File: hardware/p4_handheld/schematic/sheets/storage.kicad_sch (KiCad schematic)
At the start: 0 parts

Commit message: hw(p4_handheld): audio, storage, debug sheets
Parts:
- added J4: microSD-pushpush, TF-015, symbol PSP4H:Block2
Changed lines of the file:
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@@
     (comment 2 "Same-net labels connect; globals cross sheets")
   )
+  (symbol (lib_id "PSP4H:Block2") (at 35 35 0) (unit 1)
+    (exclude_from_sim no) (in_bom yes) (on_board yes) (dnp no) (fields_autoplaced)
+    (property "Reference" "J4" (at 35 29 0)
+      (effects (font (size 1.27 1.27))))
+    (property "Value" "microSD-pushpush" (at 35 41 0)
+      (effects (font (size 1.27 1.27))))
+    (property "Footprint" "TF-015" (at 35 35 0)
+      (effects (font (size 1.27 1.27)) hide))
+    (property "Datasheet" "~" (at 35 35 0)
+      (effects (font (size 1.27 1.27)) hide))
+    (property "Gate" "GATE-MICROSD-FOOTPRINT" (at 35 35 0)
+      (effects (font (size 1.27 1.27)) hide))
+    (property "LCSC" "C113206" (at 35 35 0)
+      (effects (font (size 1.27 1.27)) hide))
+    (property "MPN" "TF-015" (at 35 35 0)
+      (effects (font (size 1.27 1.27)) hide))
+    (instances (project "card" (path "/p4_handheld/sheets/storage" (reference "J4") (unit 1))))
+  )
+  (label "+3V3" (at 53 40 0) (fields_autoplaced)
+    (effects (font (size 1.27 1.27)) (justify left)))
+  (label "GND" (at 53 40 0) (fields_autoplaced)
+    (effects (font (size 1.27 1.27)) (justify left)))
+  (label "SD_D0" (at 53 30 0) (fields_autoplaced)
+    (effects (font (size 1.27 1.27)) (justify left)))
+  (label "SD_D1" (at 53 30 0) (fields_autoplaced)
+    (effects (font (size 1.27 1.27)) (justify left)))
+  (label "SD_D2" (at 53 30 0) (fields_autoplaced)
+    (effects (font (size 1.27 1.27)) (justify left)))
+  (label "SD_D3" (at 53 30 0) (fields_autoplaced)
+    (effects (font (size 1.27 1.27)) (justify left)))
+  (label "SD_CLK" (at 53 30 0) (fields_autoplaced)
+    (effects (font (size 1.27 1.27)) (justify left)))
+  (label "SD_CMD" (at 53 30 0) (fields_autoplaced)
+    (effects (font (size 1.27 1.27)) (justify left)))
+  (global_label "+3V3" (shape input) (at 280 20 0) (fields_autoplaced)
+    (effects (font (size 1.27 1.27)) (justify left))
+    (property "Intersheetrefs" "${INTERSHEET_REFS}" (at 280 20 0)
+      (effects (font (size 1.27 1.27)) hide))
+  )
+  (global_label "GND" (shape input) (at 280 26 0) (fields_autoplaced)
+    (effects (font (size 1.27 1.27)) (justify left))
+    (property "Intersheetrefs" "${INTERSHEET_REFS}" (at 280 26 0)
+      (effects (font (size 1.27 1.27)) hide))
+  )
+  (global_label "SD_D0" (shape input) (at 280 32 0) (fields_autoplaced)
+    (effects (font (size 1.27 1.27)) (justify left))
+    (property "Intersheetrefs" "${INTERSHEET_REFS}" (at 280 32 0)
+      (effects (font (size 1.27 1.27)) hide))
+  )
+  (global_label "SD_D1" (shape input) (at 280 38 0) (fields_autoplaced)
+    (effects (font (size 1.27 1.27)) (justify left))
+    (property "Intersheetrefs" "${INTERSHEET_REFS}" (at 280 38 0)
+      (effects (font (size 1.27 1.27)) hide))
+  )
+  (global_label "SD_D2" (shape input) (at 280 44 0) (fields_autoplaced)
+    (effects (font (size 1.27 1.27)) (justify left))
+    (property "Intersheetrefs" "${INTERSHEET_REFS}" (at 280 44 0)
+      (effects (font (size 1.27 1.27)) hide))
+  )
+  (global_label "SD_D3" (shape input) (at 280 50 0) (fields_autoplaced)
+    (effects (font (size 1.27 1.27)) (justify left))
+    (property "Intersheetrefs" "${INTERSHEET_REFS}" (at 280 50 0)
+      (effects (font (size 1.27 1.27)) hide))
+  )
+  (global_label "SD_CLK" (shape input) (at 280 56 0) (fields_autoplaced)
+    (effects (font (size 1.27 1.27)) (justify left))
+    (property "Intersheetrefs" "${INTERSHEET_REFS}" (at 280 56 0)
+      (effects (font (size 1.27 1.27)) hide))
+  )
+  (global_label "SD_CMD" (shape input) (at 280 62 0) (fields_autoplaced)
+    (effects (font (size 1.27 1.27)) (justify left))
+    (property "Intersheetrefs" "${INTERSHEET_REFS}" (at 280 62 0)
+      (effects (font (size 1.27 1.27)) hide))
+  )
 )

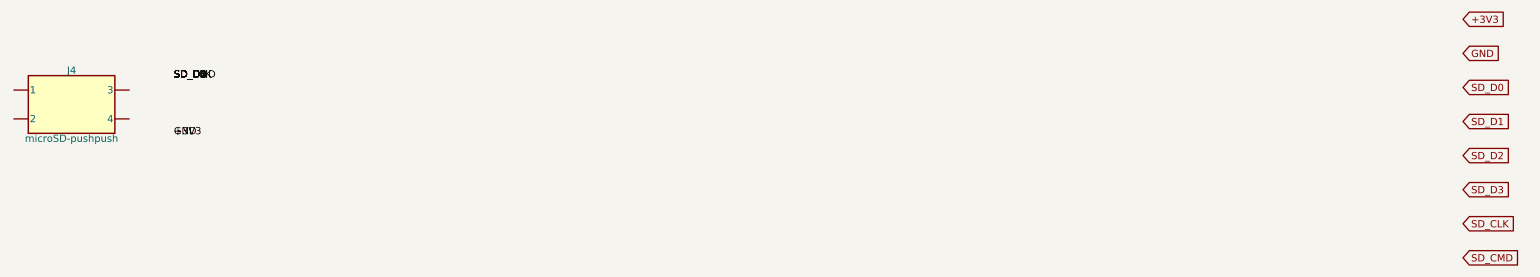
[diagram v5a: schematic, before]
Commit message: hw(p4_handheld): ERC-clean schematic engine (real pins, on-endpoint labels, project symbol lib)
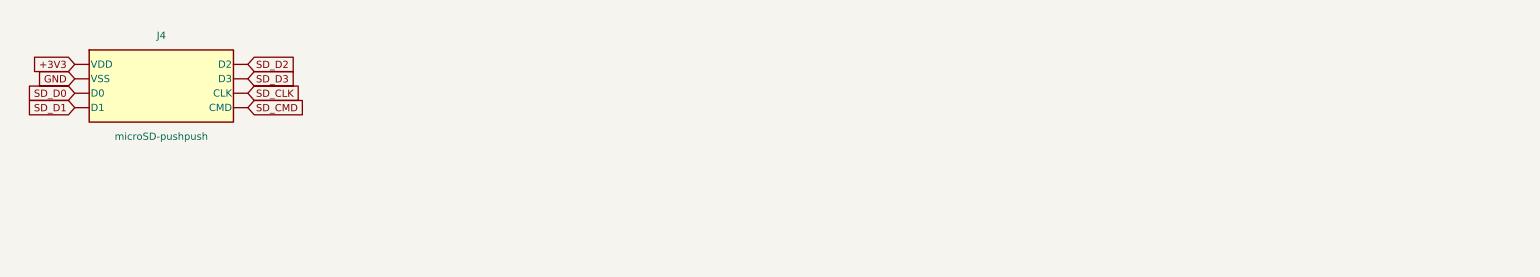
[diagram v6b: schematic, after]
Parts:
- removed J4: microSD-pushpush, TF-015, symbol PSP4H:Block2
- added J4: microSD-pushpush, symbol PSP4H:SYM_J4
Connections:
- net +3V3: now also J4.VDD
- net SD_CLK: now also J4.CLK
- new net GND: J4.VSS
- new net SD_CMD: J4.CMD
- new net SD_D0: J4.D0
- new net SD_D1: J4.D1
- new net SD_D2: J4.D2
- new net SD_D3: J4.D3
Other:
- title: PuzzleScript Card — storage -> PuzzleScript P4 Handheld — storage
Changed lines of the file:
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@@
   (generator "PuzzleScript generate_kicad.js")
   (generator_version "1.0")
-  (paper "A4")
+  (paper "A3")
   (title_block
-    (title "PuzzleScript Card — storage")
+    (title "PuzzleScript P4 Handheld — storage")
     (date "2026-07-12")
-    (rev "spin1")
+    (rev "circuit-phase-0")
     (comment 1 "Auto-generated from connectivity.json")
-    (comment 2 "Same-net labels connect; globals cross sheets")
+    (comment 2 "Labels sit on pin endpoints; globals cross sheets")
   )
-  (symbol (lib_id "PSP4H:Block2") (at 35 35 0) (unit 1)
-    (exclude_from_sim no) (in_bom yes) (on_board yes) (dnp no) (fields_autoplaced)
-    (property "Reference" "J4" (at 35 29 0)
+  (symbol (lib_id "PSP4H:SYM_J4") (at 50.8 31.75 0) (unit 1)
+    (exclude_from_sim no) (in_bom yes) (on_board yes) (dnp no)
+    (property "Reference" "J4" (at 50.8 22.86 0)
       (effects (font (size 1.27 1.27))))
-    (property "Value" "microSD-pushpush" (at 35 41 0)
+    (property "Value" "microSD-pushpush" (at 50.8 40.64 0)
       (effects (font (size 1.27 1.27))))
-    (property "Footprint" "TF-015" (at 35 35 0)
+    (property "Footprint" "" (at 50.8 31.75 0)
       (effects (font (size 1.27 1.27)) hide))
-    (property "Datasheet" "~" (at 35 35 0)
+    (property "FootprintPlan" "TF-015" (at 50.8 31.75 0)
       (effects (font (size 1.27 1.27)) hide))
-    (property "Gate" "GATE-MICROSD-FOOTPRINT" (at 35 35 0)
+    (property "Datasheet" "~" (at 50.8 31.75 0)
       (effects (font (size 1.27 1.27)) hide))
-    (property "LCSC" "C113206" (at 35 35 0)
+    (property "Gate" "GATE-MICROSD-FOOTPRINT" (at 50.8 31.75 0)
       (effects (font (size 1.27 1.27)) hide))
-    (property "MPN" "TF-015" (at 35 35 0)
+    (property "LCSC" "C113206" (at 50.8 31.75 0)
       (effects (font (size 1.27 1.27)) hide))
-    (instances (project "card" (path "/p4_handheld/sheets/storage" (reference "J4") (unit 1))))
+    (property "MPN" "TF-015" (at 50.8 31.75 0)
+      (effects (font (size 1.27 1.27)) hide))
+    (pin "VDD")
+    (pin "VSS")
+    (pin "D0")
+    (pin "D1")
+    (pin "D2")
+    (pin "D3")
+    (pin "CLK")
+    (pin "CMD")
+    (instances (project "p4_handheld" (path "/p4_handheld/sheets/storage" (reference "J4") (unit 1))))
   )
-  (label "+3V3" (at 53 40 0) (fields_autoplaced)
-    (effects (font (size 1.27 1.27)) (justify left)))
-  (label "GND" (at 53 40 0) (fields_autoplaced)
-    (effects (font (size 1.27 1.27)) (justify left)))
-  (label "SD_D0" (at 53 30 0) (fields_autoplaced)
-    (effects (font (size 1.27 1.27)) (justify left)))
-  (label "SD_D1" (at 53 30 0) (fields_autoplaced)
-    (effects (font (size 1.27 1.27)) (justify left)))
-  (label "SD_D2" (at 53 30 0) (fields_autoplaced)
-    (effects (font (size 1.27 1.27)) (justify left)))
-  (label "SD_D3" (at 53 30 0) (fields_autoplaced)
-    (effects (font (size 1.27 1.27)) (justify left)))
-  (label "SD_CLK" (at 53 30 0) (fields_autoplaced)
-    (effects (font (size 1.27 1.27)) (justify left)))
-  (label "SD_CMD" (at 53 30 0) (fields_autoplaced)
-    (effects (font (size 1.27 1.27)) (justify left)))
-  (global_label "+3V3" (shape input) (at 280 20 0) (fields_autoplaced)
-    (effects (font (size 1.27 1.27)) (justify left))
-    (property "Intersheetrefs" "${INTERSHEET_REFS}" (at 280 20 0)
+  (global_label "+3V3" (shape input) (at 35.56 27.94 180) (fields_autoplaced)
+    (effects (font (size 1.27 1.27)) (justify right))
+    (property "Intersheetrefs" "${INTERSHEET_REFS}" (at 35.56 27.94 0)
       (effects (font (size 1.27 1.27)) hide))
   )
-  (global_label "GND" (shape input) (at 280 26 0) (fields_autoplaced)
-    (effects (font (size 1.27 1.27)) (justify left))
-    (property "Intersheetrefs" "${INTERSHEET_REFS}" (at 280 26 0)
+  (global_label "GND" (shape input) (at 35.56 30.48 180) (fields_autoplaced)
+    (effects (font (size 1.27 1.27)) (justify right))
+    (property "Intersheetrefs" "${INTERSHEET_REFS}" (at 35.56 30.48 0)
       (effects (font (size 1.27 1.27)) hide))
   )
-  (global_label "SD_D0" (shape input) (at 280 32 0) (fields_autoplaced)
-    (effects (font (size 1.27 1.27)) (justify left))
-    (property "Intersheetrefs" "${INTERSHEET_REFS}" (at 280 32 0)
+  (global_label "SD_D0" (shape input) (at 35.56 33.02 180) (fields_autoplaced)
+    (effects (font (size 1.27 1.27)) (justify right))
+    (property "Intersheetrefs" "${INTERSHEET_REFS}" (at 35.56 33.02 0)
       (effects (font (size 1.27 1.27)) hide))
   )
-  (global_label "SD_D1" (shape input) (at 280 38 0) (fields_autoplaced)
-    (effects (font (size 1.27 1.27)) (justify left))
-    (property "Intersheetrefs" "${INTERSHEET_REFS}" (at 280 38 0)
+  (global_label "SD_D1" (shape input) (at 35.56 35.56 180) (fields_autoplaced)
+    (effects (font (size 1.27 1.27)) (justify right))
+    (property "Intersheetrefs" "${INTERSHEET_REFS}" (at 35.56 35.56 0)
       (effects (font (size 1.27 1.27)) hide))
   )
-  (global_label "SD_D2" (shape input) (at 280 44 0) (fields_autoplaced)
+  (global_label "SD_D2" (shape input) (at 66.04 27.94 0) (fields_autoplaced)
     (effects (font (size 1.27 1.27)) (justify left))
-    (property "Intersheetrefs" "${INTERSHEET_REFS}" (at 280 44 0)
+    (property "Intersheetrefs" "${INTERSHEET_REFS}" (at 66.04 27.94 0)
       (effects (font (size 1.27 1.27)) hide))
   )
-  (global_label "SD_D3" (shape input) (at 280 50 0) (fields_autoplaced)
+  (global_label "SD_D3" (shape input) (at 66.04 30.48 0) (fields_autoplaced)
     (effects (font (size 1.27 1.27)) (justify left))
-    (property "Intersheetrefs" "${INTERSHEET_REFS}" (at 280 50 0)
+    (property "Intersheetrefs" "${INTERSHEET_REFS}" (at 66.04 30.48 0)
       (effects (font (size 1.27 1.27)) hide))
   )
-  (global_label "SD_CLK" (shape input) (at 280 56 0) (fields_autoplaced)
+  (global_label "SD_CLK" (shape input) (at 66.04 33.02 0) (fields_autoplaced)
     (effects (font (size 1.27 1.27)) (justify left))
-    (property "Intersheetrefs" "${INTERSHEET_REFS}" (at 280 56 0)
+    (property "Intersheetrefs" "${INTERSHEET_REFS}" (at 66.04 33.02 0)
       (effects (font (size 1.27 1.27)) hide))
   )
-  (global_label "SD_CMD" (shape input) (at 280 62 0) (fields_autoplaced)
+  (global_label "SD_CMD" (shape input) (at 66.04 35.56 0) (fields_autoplaced)
     (effects (font (size 1.27 1.27)) (justify left))
-    (property "Intersheetrefs" "${INTERSHEET_REFS}" (at 280 62 0)
+    (property "Intersheetrefs" "${INTERSHEET_REFS}" (at 66.04 35.56 0)
       (effects (font (size 1.27 1.27)) hide))
   )
